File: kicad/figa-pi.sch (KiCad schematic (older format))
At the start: 4 parts

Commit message: Removed footprint for unused components Updated 3d model for LQFP-144 Updated symbol library Updated schematics Updated PCB - finished routing
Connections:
- wire segments 0 -> 3
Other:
- note added: "External \nconnections"
- note added: "PHY"
- note added: "POWER SUPLIES"
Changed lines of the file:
@@
 EESchema Schematic File Version 2
 LIBS:figa-pi
+LIBS:graphic_symbols
 LIBS:figa-pi-cache
 EELAYER 25 0
 EELAYER END
-$Descr A3 16535 11693
+$Descr A4 11693 8268
 encoding utf-8
 Sheet 1 4
@@
 L Mechanical:Mounting_Hole H1
 U 1 1 5834BC4A
-P 1950 6250
-F 0 "H1" H 1800 6350 60  0000 C CNN
-F 1 "3mm_Mounting_Hole" H 1950 6100 60  0000 C CNN
-F 2 "project_footprints:NPTH_3mm_ID" H 1850 6250 60  0001 C CNN
-F 3 "" H 1850 6250 60  0001 C CNN
-F 4 "" H -16300 -4400 50  0001 C CNN "MFR"
-F 5 "" H -16300 -4400 50  0001 C CNN "MPN"
-F 6 "" H -16300 -4400 50  0001 C CNN "SPR"
-F 7 "" H -16300 -4400 50  0001 C CNN "SPN"
-F 8 "" H -16300 -4400 50  0001 C CNN "SPURL"
-	1    1950 6250
+P 8850 5200
+F 0 "H1" H 8700 5300 60  0000 C CNN
+F 1 "3mm_Mounting_Hole" H 8850 5050 60  0000 C CNN
+F 2 "project_footprints:NPTH_3mm_ID" H 8750 5200 60  0001 C CNN
+F 3 "" H 8750 5200 60  0001 C CNN
+F 4 "" H -9400 -5450 50  0001 C CNN "MFR"
+F 5 "" H -9400 -5450 50  0001 C CNN "MPN"
+F 6 "" H -9400 -5450 50  0001 C CNN "SPR"
+F 7 "" H -9400 -5450 50  0001 C CNN "SPN"
+F 8 "" H -9400 -5450 50  0001 C CNN "SPURL"
+	1    8850 5200
 	1    0    0    -1
 $EndComp
@@
 L Mechanical:Mounting_Hole H3
 U 1 1 5834BCDF
-P 2950 6250
-F 0 "H3" H 2800 6350 60  0000 C CNN
-F 1 "3mm_Mounting_Hole" H 2950 6100 60  0000 C CNN
-F 2 "project_footprints:NPTH_3mm_ID" H 2850 6250 60  0001 C CNN
-F 3 "" H 2850 6250 60  0001 C CNN
-F 4 "" H -16300 -4400 50  0001 C CNN "MFR"
-F 5 "" H -16300 -4400 50  0001 C CNN "MPN"
-F 6 "" H -16300 -4400 50  0001 C CNN "SPR"
-F 7 "" H -16300 -4400 50  0001 C CNN "SPN"
-F 8 "" H -16300 -4400 50  0001 C CNN "SPURL"
-	1    2950 6250
+P 9850 5200
+F 0 "H3" H 9700 5300 60  0000 C CNN
+F 1 "3mm_Mounting_Hole" H 9850 5050 60  0000 C CNN
+F 2 "project_footprints:NPTH_3mm_ID" H 9750 5200 60  0001 C CNN
+F 3 "" H 9750 5200 60  0001 C CNN
+F 4 "" H -9400 -5450 50  0001 C CNN "MFR"
+F 5 "" H -9400 -5450 50  0001 C CNN "MPN"
+F 6 "" H -9400 -5450 50  0001 C CNN "SPR"
+F 7 "" H -9400 -5450 50  0001 C CNN "SPN"
+F 8 "" H -9400 -5450 50  0001 C CNN "SPURL"
+	1    9850 5200
 	1    0    0    -1
 $EndComp
@@
 L Mechanical:Mounting_Hole H2
 U 1 1 5834BD62
-P 1950 6800
-F 0 "H2" H 1800 6900 60  0000 C CNN
-F 1 "3mm_Mounting_Hole" H 1950 6650 60  0000 C CNN
-F 2 "project_footprints:NPTH_3mm_ID" H 1850 6800 60  0001 C CNN
-F 3 "" H 1850 6800 60  0001 C CNN
-F 4 "" H -16300 -4400 50  0001 C CNN "MFR"
-F 5 "" H -16300 -4400 50  0001 C CNN "MPN"
-F 6 "" H -16300 -4400 50  0001 C CNN "SPR"
-F 7 "" H -16300 -4400 50  0001 C CNN "SPN"
-F 8 "" H -16300 -4400 50  0001 C CNN "SPURL"
-	1    1950 6800
+P 8850 5750
+F 0 "H2" H 8700 5850 60  0000 C CNN
+F 1 "3mm_Mounting_Hole" H 8850 5600 60  0000 C CNN
+F 2 "project_footprints:NPTH_3mm_ID" H 8750 5750 60  0001 C CNN
+F 3 "" H 8750 5750 60  0001 C CNN
+F 4 "" H -9400 -5450 50  0001 C CNN "MFR"
+F 5 "" H -9400 -5450 50  0001 C CNN "MPN"
+F 6 "" H -9400 -5450 50  0001 C CNN "SPR"
+F 7 "" H -9400 -5450 50  0001 C CNN "SPN"
+F 8 "" H -9400 -5450 50  0001 C CNN "SPURL"
+	1    8850 5750
 	1    0    0    -1
 $EndComp
@@
 L Mechanical:Mounting_Hole H4
 U 1 1 5834BDED
-P 3000 6800
-F 0 "H4" H 2850 6900 60  0000 C CNN
-F 1 "3mm_Mounting_Hole" H 3000 6650 60  0000 C CNN
-F 2 "project_footprints:NPTH_3mm_ID" H 2900 6800 60  0001 C CNN
-F 3 "" H 2900 6800 60  0001 C CNN
-F 4 "" H -16300 -4400 50  0001 C CNN "MFR"
-F 5 "" H -16300 -4400 50  0001 C CNN "MPN"
-F 6 "" H -16300 -4400 50  0001 C CNN "SPR"
-F 7 "" H -16300 -4400 50  0001 C CNN "SPN"
-F 8 "" H -16300 -4400 50  0001 C CNN "SPURL"
-	1    3000 6800
+P 9900 5750
+F 0 "H4" H 9750 5850 60  0000 C CNN
+F 1 "3mm_Mounting_Hole" H 9900 5600 60  0000 C CNN
+F 2 "project_footprints:NPTH_3mm_ID" H 9800 5750 60  0001 C CNN
+F 3 "" H 9800 5750 60  0001 C CNN
+F 4 "" H -9400 -5450 50  0001 C CNN "MFR"
+F 5 "" H -9400 -5450 50  0001 C CNN "MPN"
+F 6 "" H -9400 -5450 50  0001 C CNN "SPR"
+F 7 "" H -9400 -5450 50  0001 C CNN "SPN"
+F 8 "" H -9400 -5450 50  0001 C CNN "SPURL"
+	1    9900 5750
 	1    0    0    -1
 $EndComp
-Text Notes 1600 5950 0    118  ~ 24
+Text Notes 8500 4900 0    118  ~ 24
 Mounting Holes
 $Sheet
-S 4050 2050 3300 1500
+S 1650 1400 2800 2100
 U 5B0D73F1
 F0 "interface.sch" 60
 F1 "interface.sch" 60
+F2 "PHY_25M" O R 4450 2850 60
+F3 "CONF_DONE" I R 4450 2450 60
+F4 "USER_LED0" O R 4450 3200 60
 $EndSheet
 $Sheet
-S 8150 2050 4200 1500
-U 5B0D756D
-F0 "ethernet.sch" 60
-F1 "ethernet.sch" 60
-$EndSheet
-$Sheet
-S 6700 4650 3950 1650
+S 1650 4300 2800 1400
 U 5B0DA588
 F0 "power.sch" 60
 F1 "power.sch" 60
 $EndSheet
+Text Notes 1900 5150 0    197  ~ 0
+POWER SUPLIES
+Wire Wire Line
+	4450 2450 6500 2450
+Wire Wire Line
+	4450 2850 6500 2850
+Text Notes 2250 2250 0    197  ~ 0
+External \nconnections
+Text Notes 7250 2200 0    197  ~ 0
+PHY
+Wire Wire Line
+	4450 3200 6500 3200
+$Sheet
+S 6500 1400 1950 2100
+U 5B0D756D
+F0 "ethernet.sch" 60
+F1 "ethernet.sch" 60
+F2 "CONF_DONE" O L 6500 2450 60
+F3 "PHY_25M" I L 6500 2850 60
+F4 "USER_LED0" I L 6500 3200 60
+$EndSheet
 $EndSCHEMATC

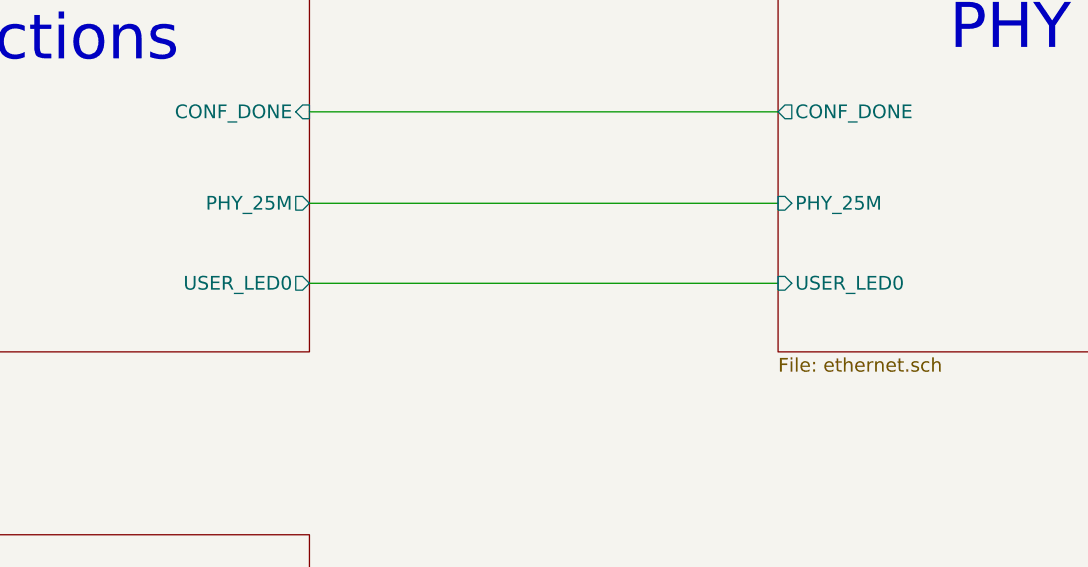
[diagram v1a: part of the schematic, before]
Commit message: Add datasheets for new components (Leds, Button, TestPoint) Add 3D models for new components (Leds, Button, TestPoint) Add footprints for new components (Leds, Button, TestPoint) Add new components to schematic library.
Schematic changes:
Change revision 1.0 -> 2.0
Add dual-color and RGB leds. Connect to FPGA.
Add tespoint for GND connection.
Add 2 tactile smd button. Connect to FPGA.
Remove User Gpio Header.
Reconnect FPGA-to-Raspberry connections

PCB changes:
Change revision 1.0 -> 2.0
Rotate RJ-45 connector
Remove text REF around fidusial.
Place new components (Leds, Button, TestPoint)
All connections routed
DRC ok (one error for fidusial)
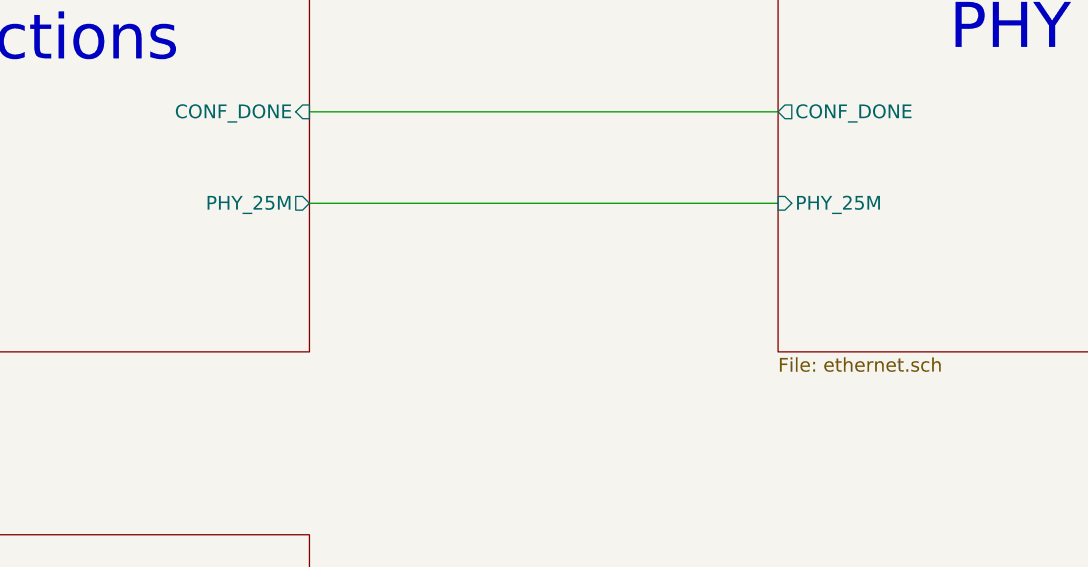
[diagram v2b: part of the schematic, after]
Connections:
- wire segments 3 -> 2
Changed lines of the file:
@@
 LIBS:figa-pi
 LIBS:graphic_symbols
+LIBS:device
+LIBS:switches
 LIBS:figa-pi-cache
 EELAYER 25 0
@@
 Title "Figa-Pi"
 Date ""
-Rev "1.0"
+Rev "2.0"
 Comp "GENERAL RnD"
-Comment1 "07e20003"
+Comment1 "07e20003-02"
 Comment2 "I. Pototskiy"
 Comment3 ""
@@
 F2 "PHY_25M" O R 4450 2850 60
 F3 "CONF_DONE" I R 4450 2450 60
-F4 "USER_LED0" O R 4450 3200 60
 $EndSheet
 $Sheet
@@
 Text Notes 7250 2200 0    197  ~ 0
 PHY
-Wire Wire Line
-	4450 3200 6500 3200
 $Sheet
 S 6500 1400 1950 2100
@@
 F2 "CONF_DONE" O L 6500 2450 60
 F3 "PHY_25M" I L 6500 2850 60
-F4 "USER_LED0" I L 6500 3200 60
 $EndSheet
 $EndSCHEMATC
